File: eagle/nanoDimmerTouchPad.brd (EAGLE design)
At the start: 40.6 x 40.6 mm, 12 parts

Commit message: change indicator LED resistor from 100 to 4700 ohm to match Legrand Adorne brightness
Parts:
- R1: value 100Ω -> 4k7Ω
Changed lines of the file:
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@@
 <attribute name="VALUE" x="20.32" y="25.4" size="0.6096" layer="27" align="bottom-center"/>
 </element>
-<element name="R1" library="rcl" library_urn="urn:adsk.eagle:library:334" package="0204/7" package3d_urn="urn:adsk.eagle:package:23498/2" value="100Ω" x="20.32" y="5.08" smashed="yes">
+<element name="R1" library="rcl" library_urn="urn:adsk.eagle:library:334" package="0204/7" package3d_urn="urn:adsk.eagle:package:23498/2" value="4k7Ω" x="20.32" y="5.08" smashed="yes">
 <attribute name="NAME" x="17.78" y="12.7" size="0.6096" layer="25" ratio="10"/>
 <attribute name="SPICEPREFIX" value="R" x="50.8" y="-19.05" size="1.778" layer="27" display="off"/>

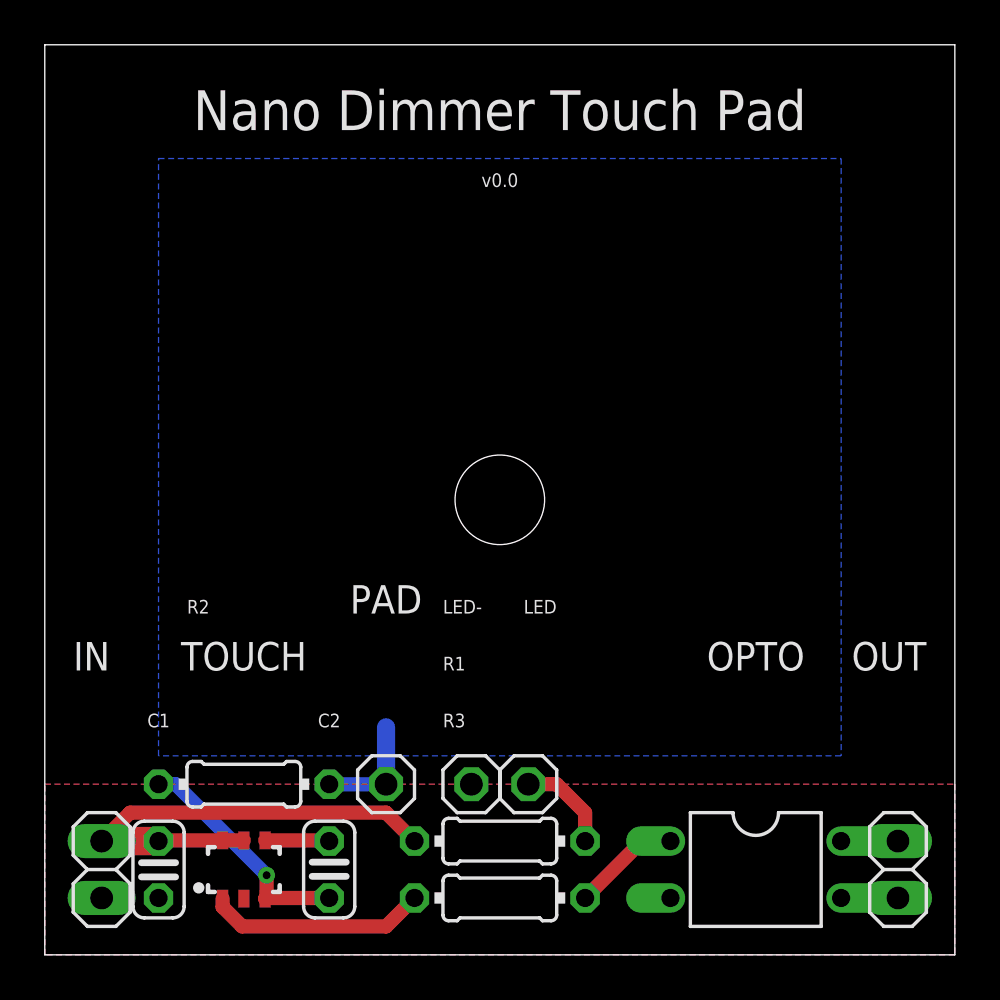
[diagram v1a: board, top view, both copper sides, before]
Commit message: v1.0: paranoid isolation of sense circuits, no ground planes, SMD resistors and capacitors
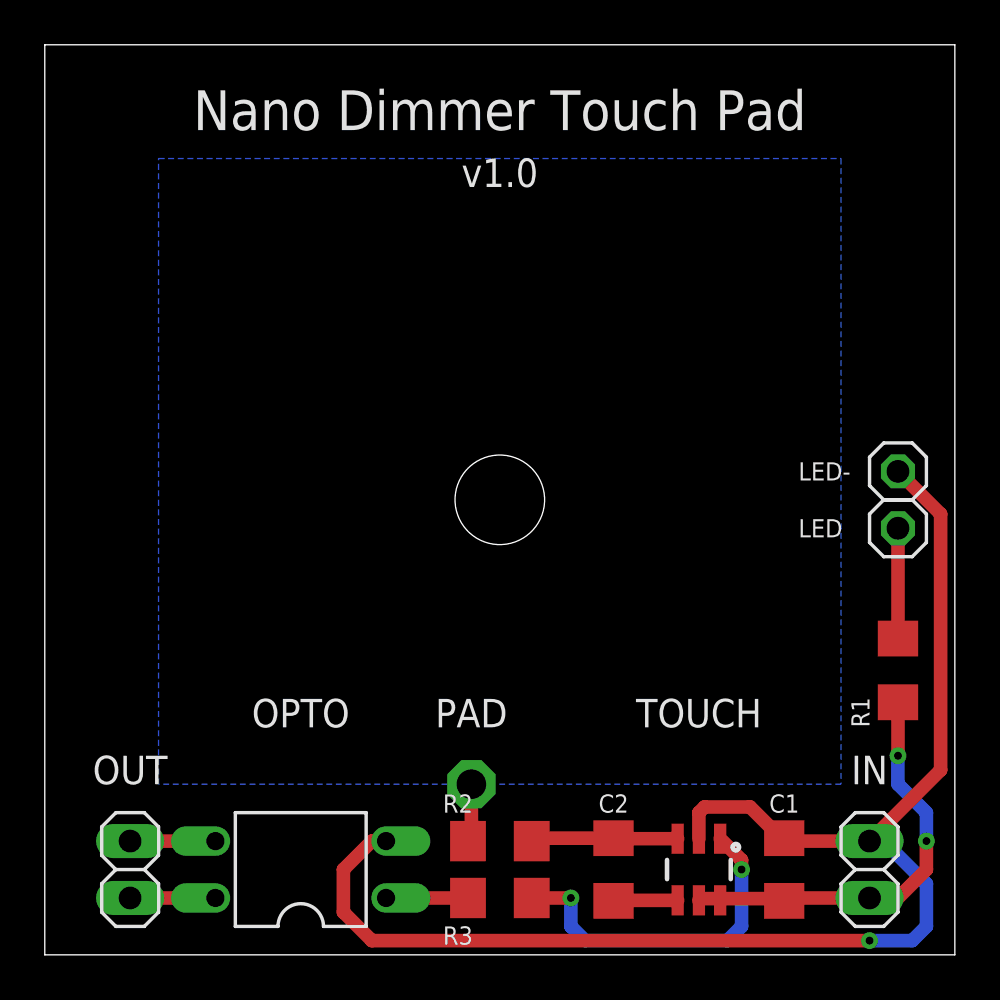
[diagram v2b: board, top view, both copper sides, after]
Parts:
- C1, C2: device rcl:C025-024X044 -> rcl:C1206
- IN: value 3V3,GND -> 3V3 GND
- OUT: value S1,COM -> S1 COM
- PAD: value PAD -> TPSQPAD1-13; device pinhead:1X01 -> testpad:P1-13
- R1, R2, R3: device rcl:0204/7 -> rcl:R1206
- TOUCH: device SparkFun-Sensors:SOT23-6 -> SparkFun-Retired:SOT23-6
- moved IN 34.3 mm to (36.8, 3.81), turned to 90 degrees
- moved OUT 34.3 mm to (3.81, 3.81), turned to 90 degrees
- moved C1 27.9 mm to (33.0, 3.81), turned to 90 degrees
- moved LED- 23.6 mm to (38.1, 21.6)
- moved OPTO 20.3 mm to (11.4, 3.81), turned to 90 degrees
- moved TOUCH 20.3 mm to (29.2, 3.81), turned to 180 degrees
- moved LED 20.1 mm to (38.1, 19.1)
- moved R1 19.3 mm to (38.1, 12.7), turned to 90 degrees
- moved C2 12.7 mm to (25.4, 3.81), turned to 270 degrees
- moved R2 11.7 mm to (20.3, 5.08), turned to 180 degrees
- moved PAD 3.81 mm to (19.1, 7.62)
- turned R3 to 180 degrees
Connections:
- net PAD: now also PAD.TP; no longer PAD.1
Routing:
- net GND: track 0.00 -> 64.7 mm, vias 0 -> 1
- net OUT: track 9.83 -> 15.5 mm, vias 0 -> 2
- net SNSK: track 10.5 -> 6.64 mm, vias 1 -> 0
- net PAD: track 5.08 -> 2.60 mm
- net 3V3: track 21.4 -> 18.9 mm, vias 0 -> 2
- net S1: track 2.54 -> 3.81 mm
- net COM: track 2.54 -> 3.81 mm
- net OPTO: track 4.86 -> 3.66 mm
- net LED: track 4.34 -> 4.93 mm
- removed copper zone on layer 1, net GND
- removed copper zone on layer 16, net GND
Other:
- board text added: "v1.0"
- board text removed: "v0.0"
